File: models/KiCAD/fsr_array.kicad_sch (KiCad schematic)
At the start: 92 parts, among them J1 scanning_ref1, J10 com_adc, J11 teensy_right, J12 teensy_left, J13 com_acc2, J14 com_acc1, J15 com_acc3, J16 com_acc4, J17 usb_B, J2 scanning_ref2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

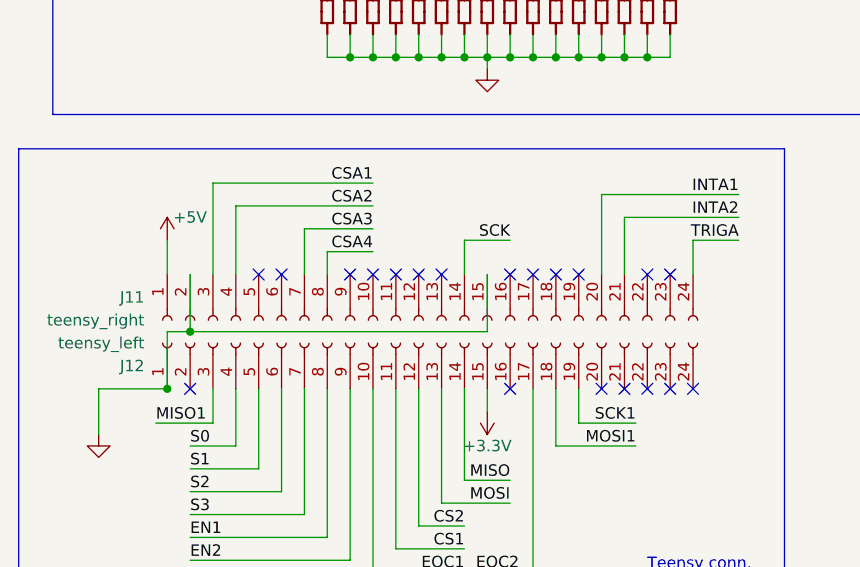
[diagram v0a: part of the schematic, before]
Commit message: fixed minor bug + added ethernet teensy code
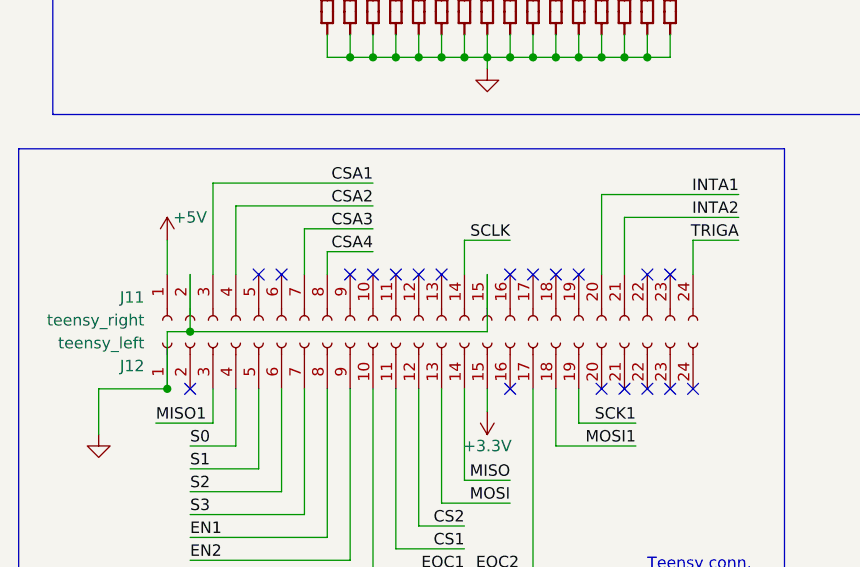
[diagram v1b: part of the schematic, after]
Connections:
- net SCK is gone; now on net SCLK: J11.14 (Pin_14)
